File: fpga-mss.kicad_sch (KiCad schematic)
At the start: 7 parts, among them U1 MPFS250T-FCVG484, Y3 Oscillator_125MHz_DSC1103DI2

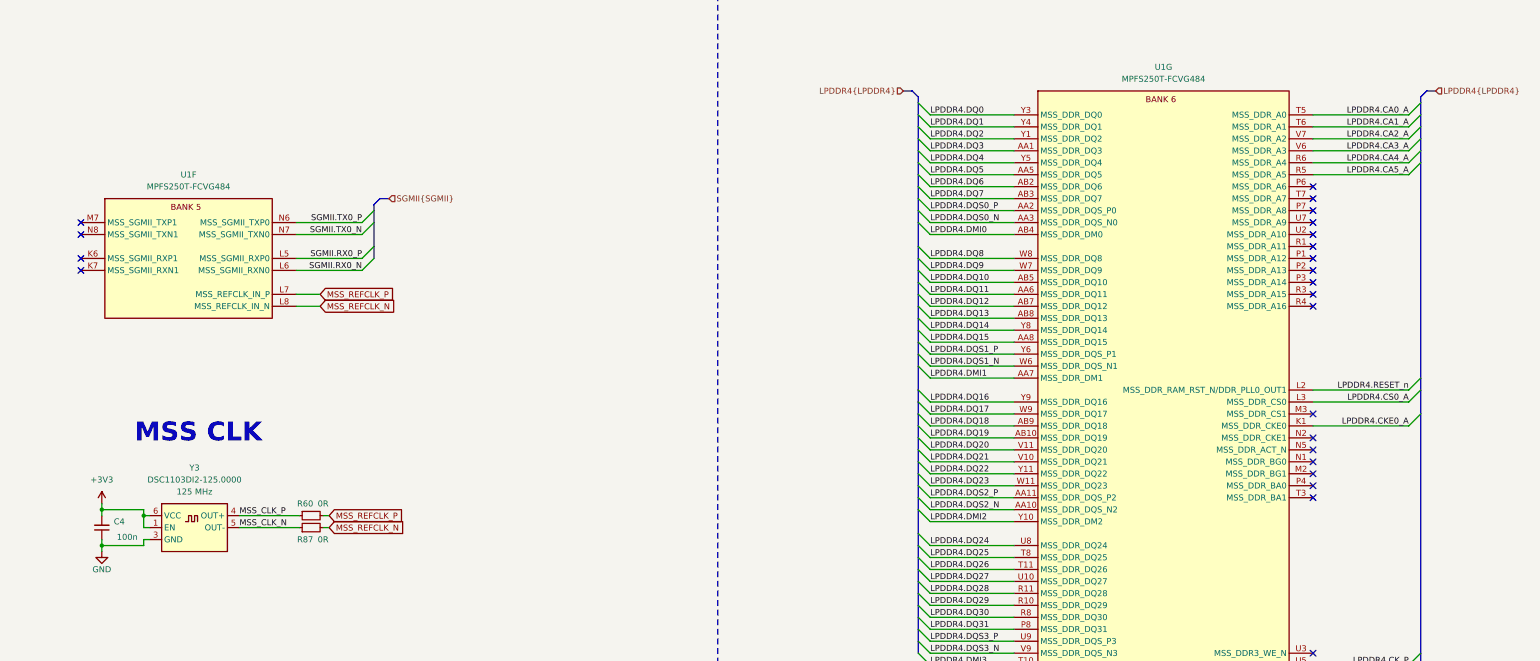
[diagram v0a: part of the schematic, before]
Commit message: [#59910] Align buses, updated symbols and clean ERC
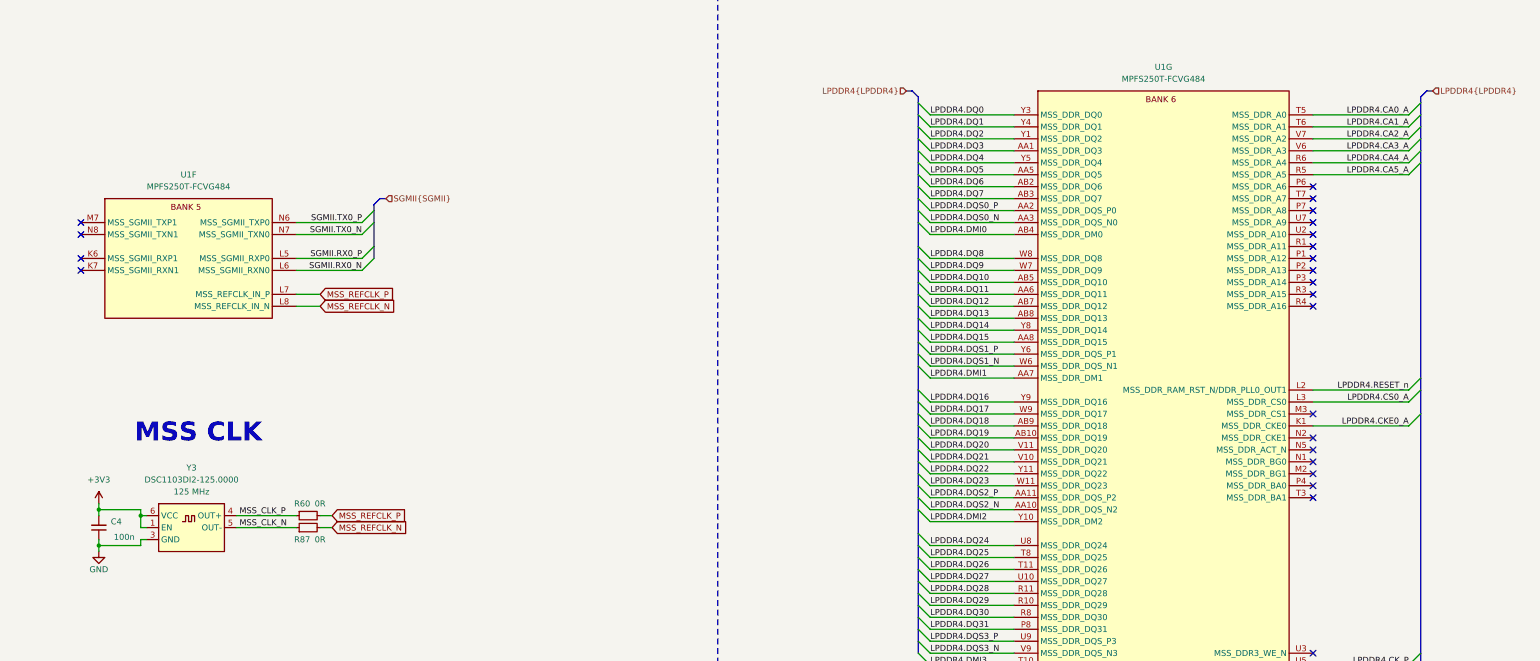
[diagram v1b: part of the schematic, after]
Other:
- moved on the sheet: C4, R60, R87, Y3
